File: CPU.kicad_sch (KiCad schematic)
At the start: 1 part

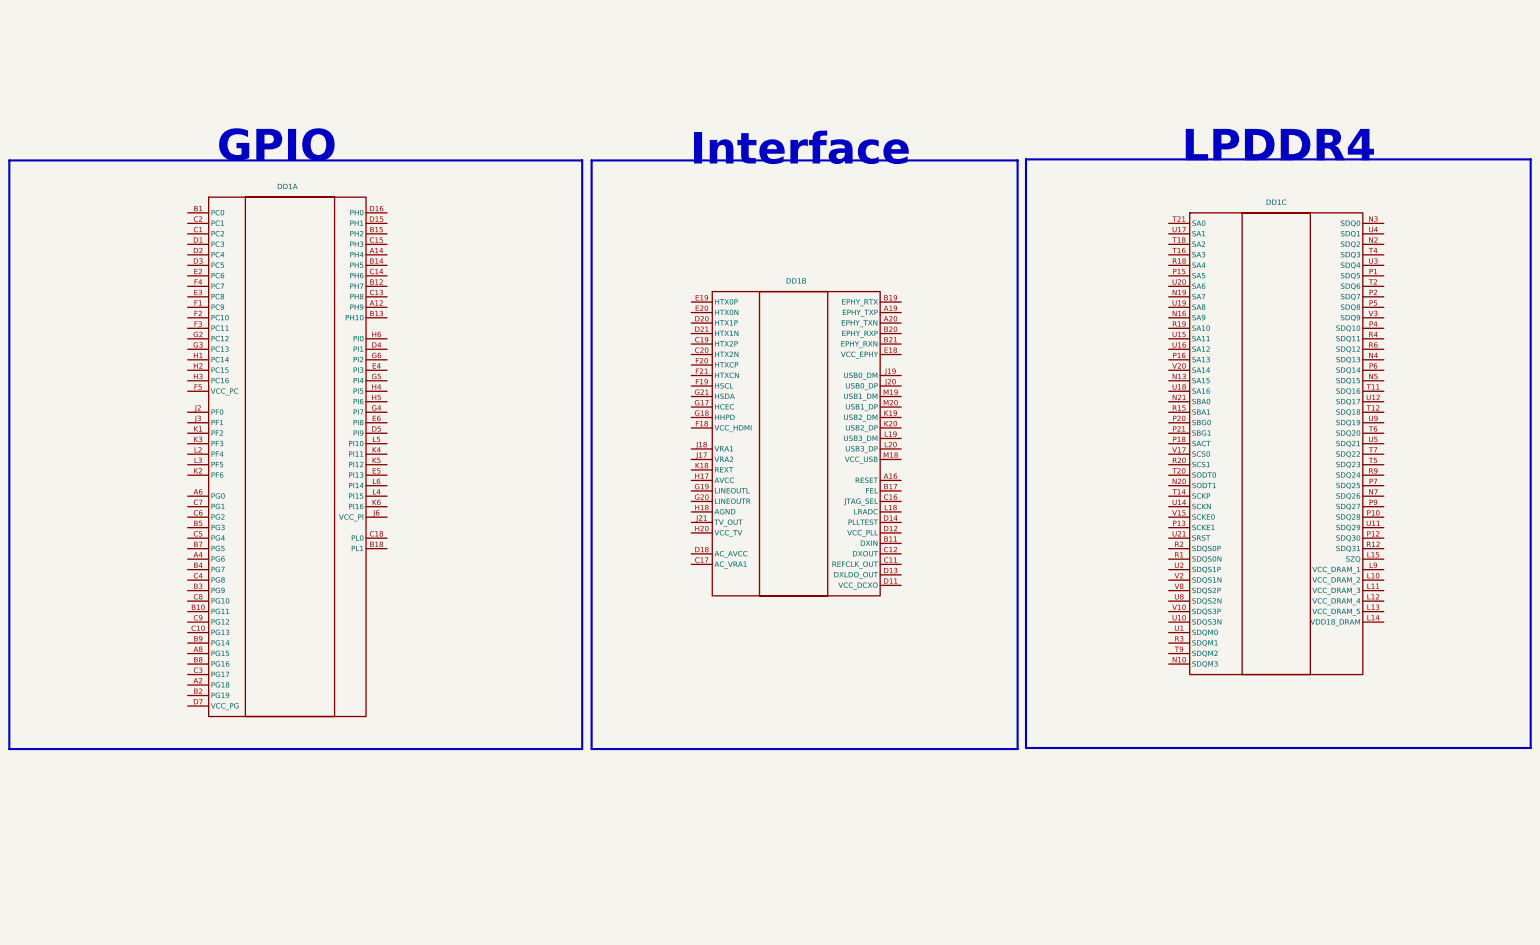
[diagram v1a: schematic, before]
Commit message: Внесены распиновки интерфейсного модуля и модуля GPIO + конденсаторы по питанию 2/7 референсной схемы
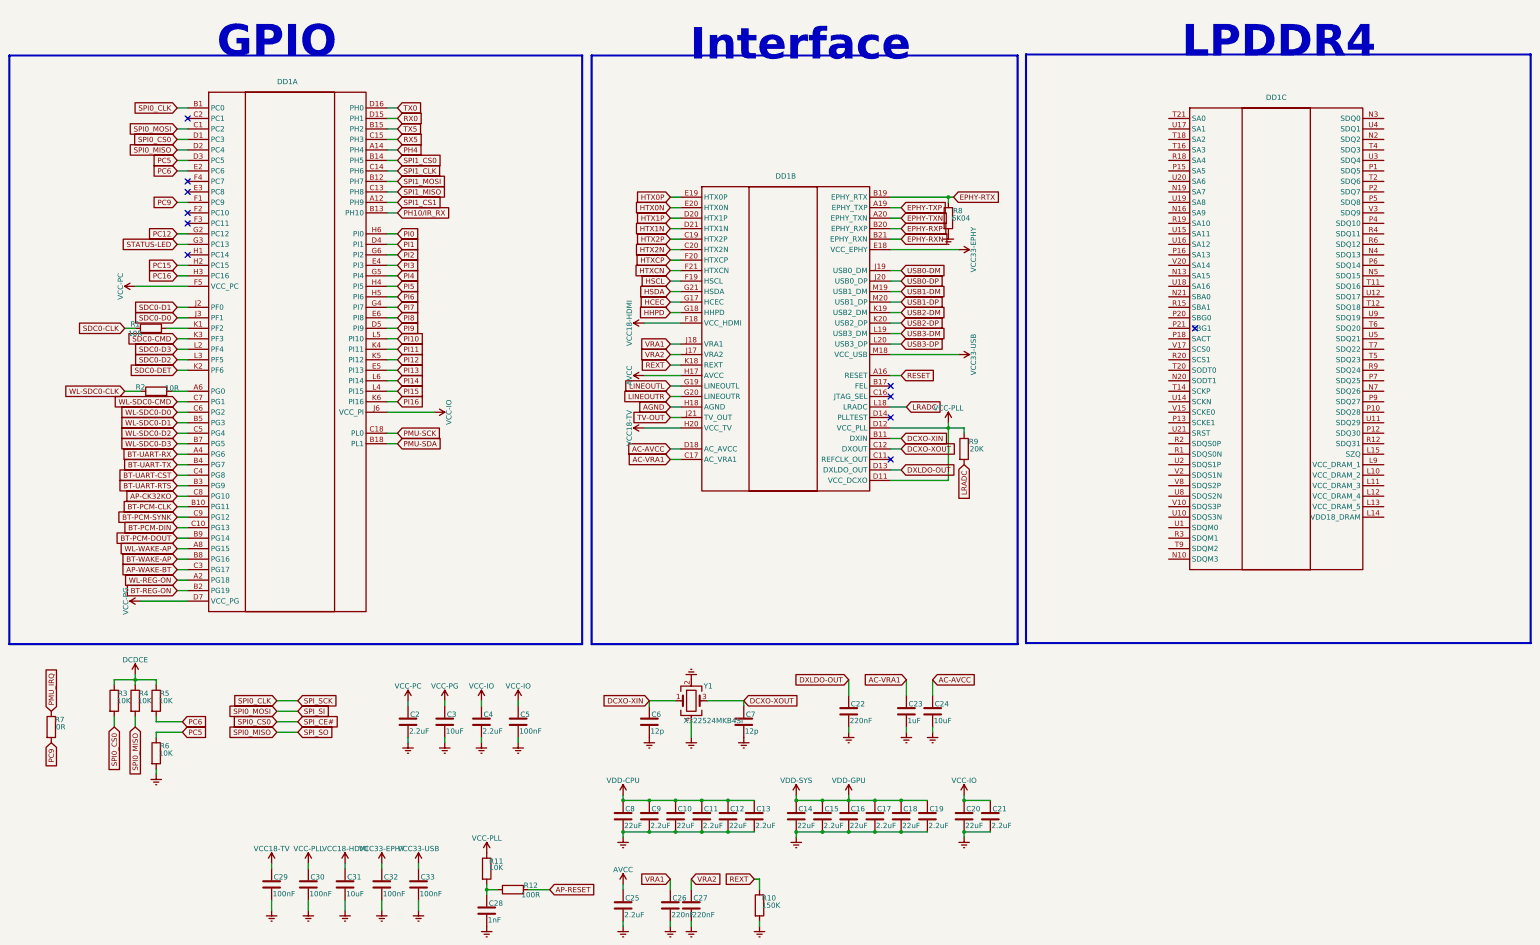
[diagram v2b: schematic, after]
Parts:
- added C10, C12, C14, C16, C18, C20, C8: 22uF, Capacitor_SMD:C_0402_1005Metric, symbol Device:C
- added C11, C13, C15, C17, C19, C2, C21, C25, C4, C9: 2.2uF, Capacitor_SMD:C_0402_1005Metric, symbol Device:C
- added C22, C26, C27: 220nF, Capacitor_SMD:C_0402_1005Metric, symbol Device:C
- added C23: 1uF, Capacitor_SMD:C_0402_1005Metric, symbol Device:C
- added C24, C3, C31: 10uF, Capacitor_SMD:C_0402_1005Metric, symbol Device:C
- added C28: 1nF, Capacitor_SMD:C_0402_1005Metric, symbol Device:C
- added C29, C30, C32, C33, C5: 100nF, Capacitor_SMD:C_0402_1005Metric, symbol Device:C
- added C6, C7: 12p, Capacitor_SMD:C_0402_1005Metric, symbol Device:C
- added R1, R2: 10R, Resistor_SMD:R_0402_1005Metric, symbol Device:R
- added R10: 150K, Resistor_SMD:R_0402_1005Metric, symbol Device:R
- added R11, R3, R4, R5, R6: 10K, Resistor_SMD:R_0402_1005Metric, symbol Device:R
- added R12: 100R, Resistor_SMD:R_0402_1005Metric, symbol Device:R
- added R7: 0R, Resistor_SMD:R_0402_1005Metric, symbol Device:R
- added R8: 6K04, Resistor_SMD:R_0402_1005Metric, symbol Device:R
- added R9: 20K, Resistor_SMD:R_0402_1005Metric, symbol Device:R
- added Y1: X322524MKB4SI, Oscillator:Oscillator_SMD_EuroQuartz_XO32-4Pin_3.2x2.5mm, symbol Device:Crystal_GND24
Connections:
- net RESET: now reaches DD1.A16 (RESET)
- net EPHY-TXP: now reaches DD1.A19 (EPHY_TXP)
- net EPHY-TXN: now reaches DD1.A20 (EPHY_TXN)
- net DCXO-XIN: now reaches DD1.B11 (DXIN)
- net DCXO-XIN: now also C6.1, Y1.1
- net EPHY-RTX: now reaches DD1.B19 (EPHY_RTX)
- net EPHY-RTX: now also R8.1
- net EPHY-RXP: now reaches DD1.B20 (EPHY_RXP)
- net EPHY-RXN: now reaches DD1.B21 (EPHY_RXN)
- net DCXO-XOUT: now reaches DD1.C12 (DXOUT)
- net DCXO-XOUT: now also C7.1, Y1.3
- net AC-VRA1: now reaches DD1.C17 (AC_VRA1)
- net AC-VRA1: now also C23.1
- net HTX2P: now reaches DD1.C19 (HTX2P)
- net HTX2N: now reaches DD1.C20 (HTX2N)
- net VCC-PLL: now reaches DD1.D11 (VCC_DCXO)
- net VCC-PLL: now also DD1.D12 (VCC_PLL), C30.1, R11.1, R9.1
- net DXLDO-OUT: now reaches DD1.D13 (DXLDO_OUT)
- net DXLDO-OUT: now also C22.1
- net AC-AVCC: now reaches DD1.D18 (AC_AVCC)
- net AC-AVCC: now also C24.1
- net HTX1P: now reaches DD1.D20 (HTX1P)
- net HTX1N: now reaches DD1.D21 (HTX1N)
- net VCC33-EPHY: now reaches DD1.E18 (VCC_EPHY)
- net VCC33-EPHY: now also C32.1
- net HTX0P: now reaches DD1.E19 (HTX0P)
- net HTX0N: now reaches DD1.E20 (HTX0N)
- net VCC18-HDMI: now reaches DD1.F18 (VCC_HDMI)
- net VCC18-HDMI: now also C31.1
- net HSCL: now reaches DD1.F19 (HSCL)
- net HTXCP: now reaches DD1.F20 (HTXCP)
- net HTXCN: now reaches DD1.F21 (HTXCN)
- net HCEC: now reaches DD1.G17 (HCEC)
- net HHPD: now reaches DD1.G18 (HHPD)
- net LINEOUTL: now reaches DD1.G19 (LINEOUTL)
- net LINEOUTR: now reaches DD1.G20 (LINEOUTR)
- net HSDA: now reaches DD1.G21 (HSDA)
- net AVCC: now reaches DD1.H17 (AVCC)
- net AVCC: now also C25.1
- net AGND: now reaches DD1.H18 (AGND)
- net VCC18-TV: now reaches DD1.H20 (VCC_TV)
- net VCC18-TV: now also C29.1
- net VRA2: now reaches DD1.J17 (VRA2)
- net VRA2: now also C27.1
- net VRA1: now reaches DD1.J18 (VRA1)
- net VRA1: now also C26.1
- net USB0-DM: now reaches DD1.J19 (USB0_DM)
- net USB0-DP: now reaches DD1.J20 (USB0_DP)
- net TV-OUT: now reaches DD1.J21 (TV_OUT)
- net REXT: now reaches DD1.K18 (REXT)
- net REXT: now also R10.1
- net USB2-DM: now reaches DD1.K19 (USB2_DM)
- net USB2-DP: now reaches DD1.K20 (USB2_DP)
- net LRADC: now reaches DD1.L18 (LRADC)
- net LRADC: now also R9.2
- net USB3-DM: now reaches DD1.L19 (USB3_DM)
- net USB3-DP: now reaches DD1.L20 (USB3_DP)
- net VCC33-USB: now reaches DD1.M18 (VCC_USB)
- net VCC33-USB: now also C33.1
- net USB1-DM: now reaches DD1.M19 (USB1_DM)
- net USB1-DP: now reaches DD1.M20 (USB1_DP)
- net SPI1_CS1: now reaches DD1.A12 (PH9)
- net PH4: now reaches DD1.A14 (PH4)
- net WL-REG-ON: now reaches DD1.A2 (PG18)
- net BT-UART-RX: now reaches DD1.A4 (PG6)
- net at DD1.A6 (PG0): now also R2.2
- net WL-WAKE-AP: now reaches DD1.A8 (PG15)
- net SPI0_CLK: now reaches DD1.B1 (PC0)
- net BT-PCM-CLK: now reaches DD1.B10 (PG11)
- net SPI1_MOSI: now reaches DD1.B12 (PH7)
- net PH10/IR_RX: now reaches DD1.B13 (PH10)
- net SPI1_CS0: now reaches DD1.B14 (PH5)
- net TX5: now reaches DD1.B15 (PH2)
- net PMU-SDA: now reaches DD1.B18 (PL1)
- net BT-REG-ON: now reaches DD1.B2 (PG19)
- net BT-UART-RTS: now reaches DD1.B3 (PG9)
- net BT-UART-TX: now reaches DD1.B4 (PG7)
- net WL-SDC0-D1: now reaches DD1.B5 (PG3)
- net WL-SDC0-D3: now reaches DD1.B7 (PG5)
- net BT-WAKE-AP: now reaches DD1.B8 (PG16)
- net BT-PCM-DOUT: now reaches DD1.B9 (PG14)
- net SPI0_MOSI: now reaches DD1.C1 (PC2)
- net BT-PCM-DIN: now reaches DD1.C10 (PG13)
- net SPI1_MISO: now reaches DD1.C13 (PH8)
- net SPI1_CLK: now reaches DD1.C14 (PH6)
- net RX5: now reaches DD1.C15 (PH3)
- net PMU-SCK: now reaches DD1.C18 (PL0)
- net AP-WAKE-BT: now reaches DD1.C3 (PG17)
- net BT-UART-CST: now reaches DD1.C4 (PG8)
- net WL-SDC0-D2: now reaches DD1.C5 (PG4)
- net WL-SDC0-D0: now reaches DD1.C6 (PG2)
- net WL-SDC0-CMD: now reaches DD1.C7 (PG1)
- net AP-CK32KO: now reaches DD1.C8 (PG10)
- net BT-PCM-SYNK: now reaches DD1.C9 (PG12)
- net SPI0_CS0: now reaches DD1.D1 (PC3)
- net SPI0_CS0: now also R3.2
- net RX0: now reaches DD1.D15 (PH1)
- net TX0: now reaches DD1.D16 (PH0)
- net SPI0_MISO: now reaches DD1.D2 (PC4)
- net SPI0_MISO: now also R4.2
- net PC5: now reaches DD1.D3 (PC5)
- net PC5: now also R6.1
- net PI1: now reaches DD1.D4 (PI1)
- net PI9: now reaches DD1.D5 (PI9)
- net VCC-PG: now reaches DD1.D7 (VCC_PG)
- net VCC-PG: now also C3.1
- net PC6: now reaches DD1.E2 (PC6)
- net PC6: now also R5.2
- net PI3: now reaches DD1.E4 (PI3)
- net PI13: now reaches DD1.E5 (PI13)
- net PI8: now reaches DD1.E6 (PI8)
- net PC9: now reaches DD1.F1 (PC9)
- net PC9: now also R7.2
- net VCC-PC: now reaches DD1.F5 (VCC_PC)
- net VCC-PC: now also C2.1
- net PC12: now reaches DD1.G2 (PC12)
- net STATUS-LED: now reaches DD1.G3 (PC13)
- net PI7: now reaches DD1.G4 (PI7)
- net PI4: now reaches DD1.G5 (PI4)
- net PI2: now reaches DD1.G6 (PI2)
- net PC15: now reaches DD1.H2 (PC15)
- net PC16: now reaches DD1.H3 (PC16)
- net PI5: now reaches DD1.H4 (PI5)
- net PI6: now reaches DD1.H5 (PI6)
- net PI0: now reaches DD1.H6 (PI0)
- net SDC0-D1: now reaches DD1.J2 (PF0)
- net SDC0-D0: now reaches DD1.J3 (PF1)
- net VCC-IO: now reaches DD1.J6 (VCC_PI)
- net VCC-IO: now also C20.1, C21.1, C4.1, C5.1
- net at DD1.K1 (PF2): now also R1.2
- net SDC0-DET: now reaches DD1.K2 (PF6)
- net SDC0-CMD: now reaches DD1.K3 (PF3)
- net PI11: now reaches DD1.K4 (PI11)
- net PI12: now reaches DD1.K5 (PI12)
- net PI16: now reaches DD1.K6 (PI16)
- net SDC0-D3: now reaches DD1.L2 (PF4)
- net SDC0-D2: now reaches DD1.L3 (PF5)
- net PI15: now reaches DD1.L4 (PI15)
- net PI10: now reaches DD1.L5 (PI10)
- net PI14: now reaches DD1.L6 (PI14)
- new net: C28.1, R11.2, R12.1
- new net AP-RESET: R12.2
- new net DCDCE: R3.1, R4.1, R5.1
- new net Earth: C10.2, C11.2, C12.2, C13.2, C14.2, C15.2, C16.2, C17.2, C18.2, C19.2, C2.2, C20.2, C21.2, C22.2, C23.2, C24.2, C25.2, C26.2, C27.2, C28.2, C29.2, C3.2, C30.2, C31.2, C32.2, C33.2, C4.2, C5.2, C6.2, C7.2, C8.2, C9.2, R10.2, R6.2, R8.2, Y1.2, Y1.4
- new net PMU_IRQ: R7.1
- new net SDC0-CLK: R1.1
- new net VDD-CPU: C10.1, C11.1, C12.1, C13.1, C8.1, C9.1
- new net VDD-GPU: C14.1, C15.1, C16.1, C17.1, C18.1, C19.1
- new net WL-SDC0-CLK: R2.1
- no-connect marks 0 -> 11
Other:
- moved on the sheet: DD1A, DD1B, DD1C

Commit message: ddr
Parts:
- added C34: 22uF, Capacitor_SMD:C_0402_1005Metric, symbol Device:C
- added C35, C37, C39, C41: 2.2uF, Capacitor_SMD:C_0402_1005Metric, symbol Device:C
- added C36, C38, C42: 1uF, Capacitor_SMD:C_0402_1005Metric, symbol Device:C
- added C40: 100nF, Capacitor_SMD:C_0402_1005Metric, symbol Device:C
- added R13: 20K, Resistor_SMD:R_0402_1005Metric, symbol Device:R
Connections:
- net Earth: now also C34.2, C35.2, C36.2, C37.2, C38.2, C39.2, C40.2, C41.2, C42.2, R13.2
- net VCC-DRAM: now reaches DD1.L10 (VCC_DRAM_2)
- net VCC-DRAM: now also DD1.L11 (VCC_DRAM_3), DD1.L12 (VCC_DRAM_4), DD1.L13 (VCC_DRAM_5), C34.1, C35.1, C36.1, C37.1, C38.1, C39.1
- net VDD18-LPDDR: now reaches DD1.L14 (VDD18_DRAM)
- net VDD18-LPDDR: now also C40.1, C41.1, C42.1
- net SDQ31: now reaches DD1.L15 (SZQ)
- net SDQ31: now also DD1.R12 (SDQ31)
- net at DD1.L9 (VCC_DRAM_1): now also R13.1
- net SDQM3: now reaches DD1.N10 (SDQM3)
- net SDQ2: now reaches DD1.N2 (SDQ2)
- net SDQ0: now reaches DD1.N3 (SDQ0)
- net SDQ13: now reaches DD1.N4 (SDQ13)
- net SDQ15: now reaches DD1.N5 (SDQ15)
- net SDQ26: now reaches DD1.N7 (SDQ26)
- net SDQ5: now reaches DD1.P1 (SDQ5)
- net SDQ28: now reaches DD1.P10 (SDQ28)
- net SDQ30: now reaches DD1.P12 (SDQ30)
- net SCKE1: now reaches DD1.P13 (SCKE1)
- net SCS1: now reaches DD1.P15 (SA5)
- net SDQ7: now reaches DD1.P2 (SDQ7)
- net SDQ10: now reaches DD1.P4 (SDQ10)
- net SDQ8: now reaches DD1.P5 (SDQ8)
- net SDQ14: now reaches DD1.P6 (SDQ14)
- net SDQ25: now reaches DD1.P7 (SDQ25)
- net SDQ27: now reaches DD1.P9 (SDQ27)
- net SDQS0N: now reaches DD1.R1 (SDQS0N)
- net SA4: now reaches DD1.R18 (SA4)
- net SDQS0P: now reaches DD1.R2 (SDQS0P)
- net SA3: now reaches DD1.R20 (SCS1)
- net SDQM1: now reaches DD1.R3 (SDQM1)
- net SDQ11: now reaches DD1.R4 (SDQ11)
- net SDQ12: now reaches DD1.R6 (SDQ12)
- net SDQ24: now reaches DD1.R9 (SDQ24)
- net SDQ16: now reaches DD1.T11 (SDQ16)
- net SDQ18: now reaches DD1.T12 (SDQ18)
- net SCKP: now reaches DD1.T14 (SCKP)
- net SA5: now reaches DD1.T16 (SA3)
- net SCS0: now reaches DD1.T18 (SA2)
- net SDQ6: now reaches DD1.T2 (SDQ6)
- net SA2: now reaches DD1.T21 (SA0)
- net SDQ3: now reaches DD1.T4 (SDQ3)
- net SDQ23: now reaches DD1.T5 (SDQ23)
- net SDQ20: now reaches DD1.T6 (SDQ20)
- net SDQ22: now reaches DD1.T7 (SDQ22)
- net SDQM2: now reaches DD1.T9 (SDQM2)
- net SDQM0: now reaches DD1.U1 (SDQM0)
- net SDQS3N: now reaches DD1.U10 (SDQS3N)
- net SDQ29: now reaches DD1.U11 (SDQ29)
- net SDQ17: now reaches DD1.U12 (SDQ17)
- net SCKN: now reaches DD1.U14 (SCKN)
- net SA0: now reaches DD1.U17 (SA1)
- net SDQS1P: now reaches DD1.U2 (SDQS1P)
- net SRST: now reaches DD1.U21 (SRST)
- net SDQ4: now reaches DD1.U3 (SDQ4)
- net SDQ1: now reaches DD1.U4 (SDQ1)
- net SDQ21: now reaches DD1.U5 (SDQ21)
- net SDQS2N: now reaches DD1.U8 (SDQS2N)
- net SDQ19: now reaches DD1.U9 (SDQ19)
- net SDQS3P: now reaches DD1.V10 (SDQS3P)
- net SCKE0: now reaches DD1.V15 (SCKE0)
- net SA1: now reaches DD1.V17 (SCS0)
- net SDQS1N: now reaches DD1.V2 (SDQS1N)
- net SDQ9: now reaches DD1.V3 (SDQ9)
- net SDQS2P: now reaches DD1.V8 (SDQS2P)
- no-connect marks 11 -> 29
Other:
- moved on the sheet: C10, C11, C12, C13, C14, C15, C16, C17, C18, C19, C2, C20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

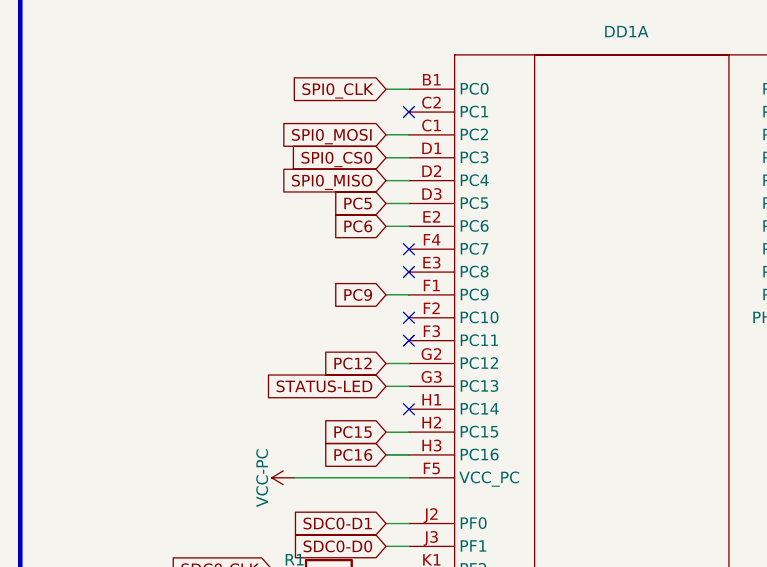
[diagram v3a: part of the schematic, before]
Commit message: Обновлена структура, закончен интерфейс, HDMI Завершено проектирование линий питания и подтяжек для интерфейсов
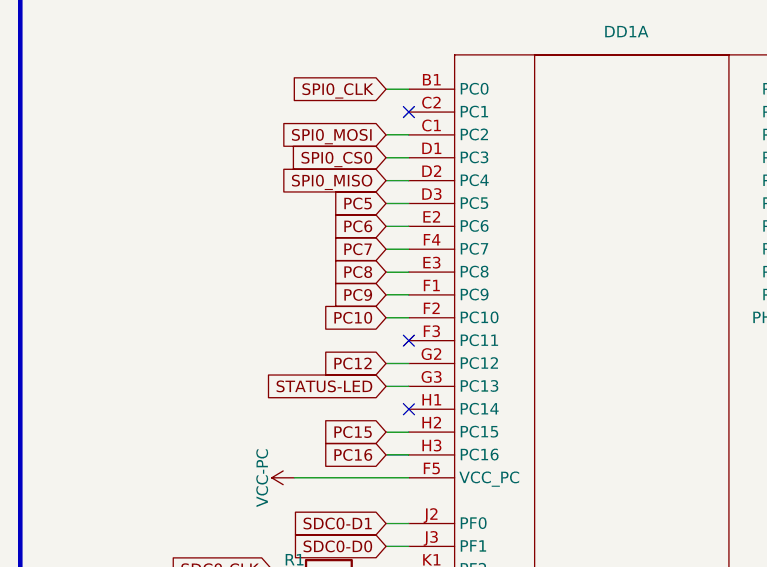
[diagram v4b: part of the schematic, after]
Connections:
- net PC8: now reaches DD1.E3 (PC8)
- net PC10: now reaches DD1.F2 (PC10)
- net PC7: now reaches DD1.F4 (PC7)
- no-connect marks 29 -> 26
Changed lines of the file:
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@@
 	)
 	(no_connect
-		(at 77.47 78.74)
-	)
-	(no_connect
 		(at 314.96 101.6)
 	)
@@
 	)
 	(no_connect
-		(at 77.47 81.28)
-	)
-	(no_connect
 		(at 314.96 83.82)
 	)
@@
 	)
 	(no_connect
-		(at 77.47 86.36)
-	)
-	(no_connect
 		(at 77.47 63.5)
 	)
@@
 	(wire
 		(pts
+			(xy 74.93 78.74) (xy 77.47 78.74)
+		)
+		(stroke
+			(width 0)
+			(type default)
+		)
+	)
+	(wire
+		(pts
 			(xy 74.93 210.82) (xy 74.93 208.28)
 		)
@@
 	(wire
 		(pts
+			(xy 74.93 86.36) (xy 77.47 86.36)
+		)
+		(stroke
+			(width 0)
+			(type default)
+		)
+	)
+	(wire
+		(pts
 			(xy 128.27 129.54) (xy 125.73 129.54)
 		)
@@
 	(wire
 		(pts
+			(xy 74.93 81.28) (xy 77.47 81.28)
+		)
+		(stroke
+			(width 0)
+			(type default)
+		)
+	)
+	(wire
+		(pts
 			(xy 247.65 100.33) (xy 250.19 100.33)
 		)
@@
 		)
 	)
+	(global_label "PC10"
+		(shape input)
+		(at 74.93 86.36 180)
+		(fields_autoplaced yes)
+		(effects
+			(font
+				(size 1.27 1.27)
+			)
+			(justify right)
+		)
+		(property "Intersheetrefs" "${INTERSHEET_REFS}"
+			(at 69.3929 86.36 0)
+			(effects
+				(font
+					(size 1.27 1.27)
+				)
+				(justify right)
+				(hide yes)
+			)
+		)
+	)
 	(global_label "USB1-DM"
 		(shape input)
@@
 		)
 	)
+	(global_label "PC8"
+		(shape input)
+		(at 74.93 81.28 180)
+		(fields_autoplaced yes)
+		(effects
+			(font
+				(size 1.27 1.27)
+			)
+			(justify right)
+		)
+		(property "Intersheetrefs" "${INTERSHEET_REFS}"
+			(at 69.9128 81.28 0)
+			(effects
+				(font
+					(size 1.27 1.27)
+				)
+				(justify right)
+				(hide yes)
+			)
+		)
+	)
 	(global_label "AC-VRA1"
 		(shape input)
@@
 			(effects
 				(font
+					(size 1.27 1.27)
+				)
+				(justify right)
+				(hide yes)
+			)
+		)
+	)
+	(global_label "PC7"
+		(shape input)
+		(at 74.93 78.74 180)
+		(fields_autoplaced yes)
+		(effects
+			(font
+				(size 1.27 1.27)
+			)
+			(justify right)
+		)
+		(property "Intersheetrefs" "${INTERSHEET_REFS}"
+			(at 69.9128 78.74 0)
+			(effects
+				(font

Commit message: Схема закончена, часть компонентов расставлена на плате
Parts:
- renumbered C29 to C23, C30 to C24, C31 to C25, C32 to C26, C2 to C27, C33 to C28, C3 to C29, C4 to C30, C28 to C31, C5 to C32, C8 to C33, C25 to C34, C6 to C35, C9 to C36, C26 to C37, C10 to C38, C27 to C39, C11 to C40, C12 to C41, C7 to C42, C13 to C43, C14 to C44, C15 to C45, C22 to C46, C16 to C47, C17 to C48, C18 to C49, C23 to C50, C19 to C51, C24 to C52, C20 to C53, C21 to C54, C34 to C55, C35 to C56, C36 to C57, C37 to C58, C38 to C59, C39 to C60, C40 to C61, C41 to C62, C42 to C63, R7 to R19, R1 to R20, R2 to R21, R3 to R22, R4 to R23, R5 to R24, R6 to R25, R11 to R26, R12 to R27, R10 to R28, R8 to R29, R9 to R30, R13 to R31
